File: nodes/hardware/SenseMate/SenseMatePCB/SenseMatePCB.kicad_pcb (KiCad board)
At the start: 2 copper layers, 40.6 x 67.8 mm, 14 parts, among them J1 Conn_01x04, M1 Motor_DC, Q1 2SC1815, Q2 2SC1815, SW5 SW_DPDT_x2

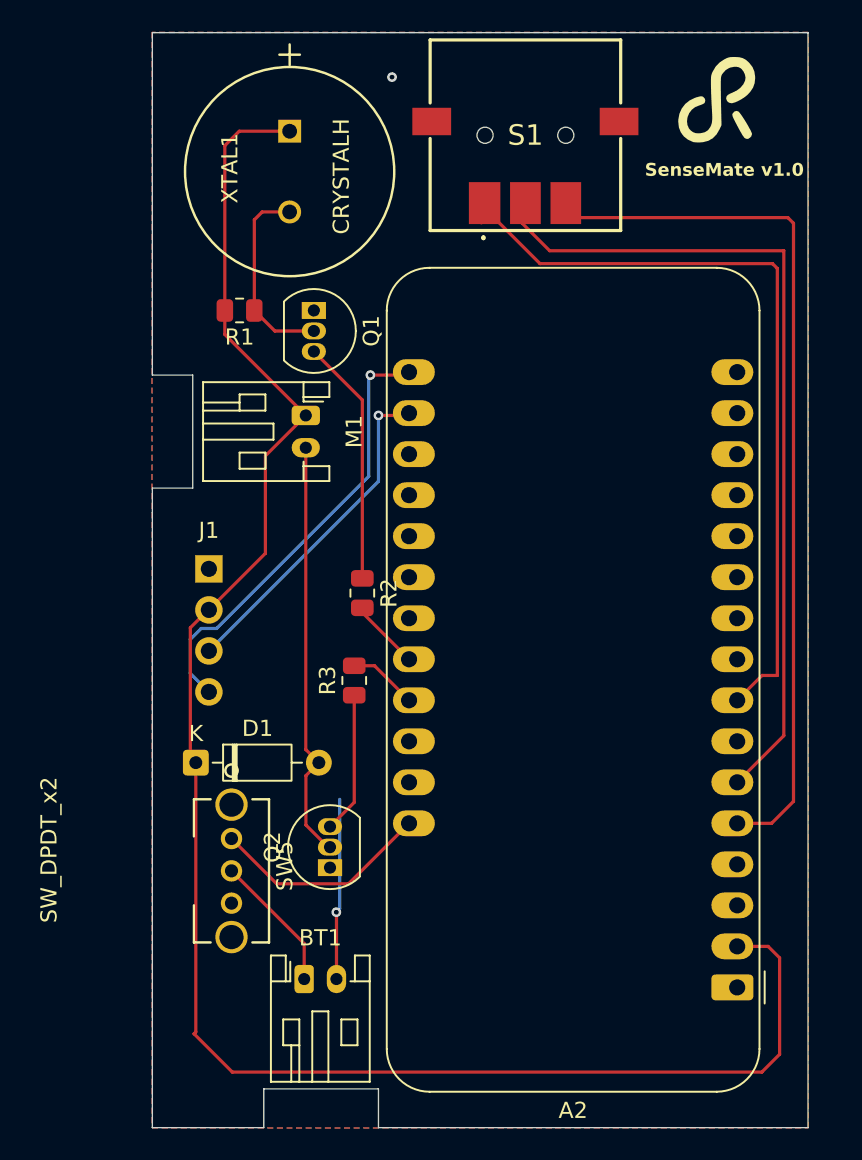
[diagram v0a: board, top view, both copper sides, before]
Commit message: some silkscreen writing movement
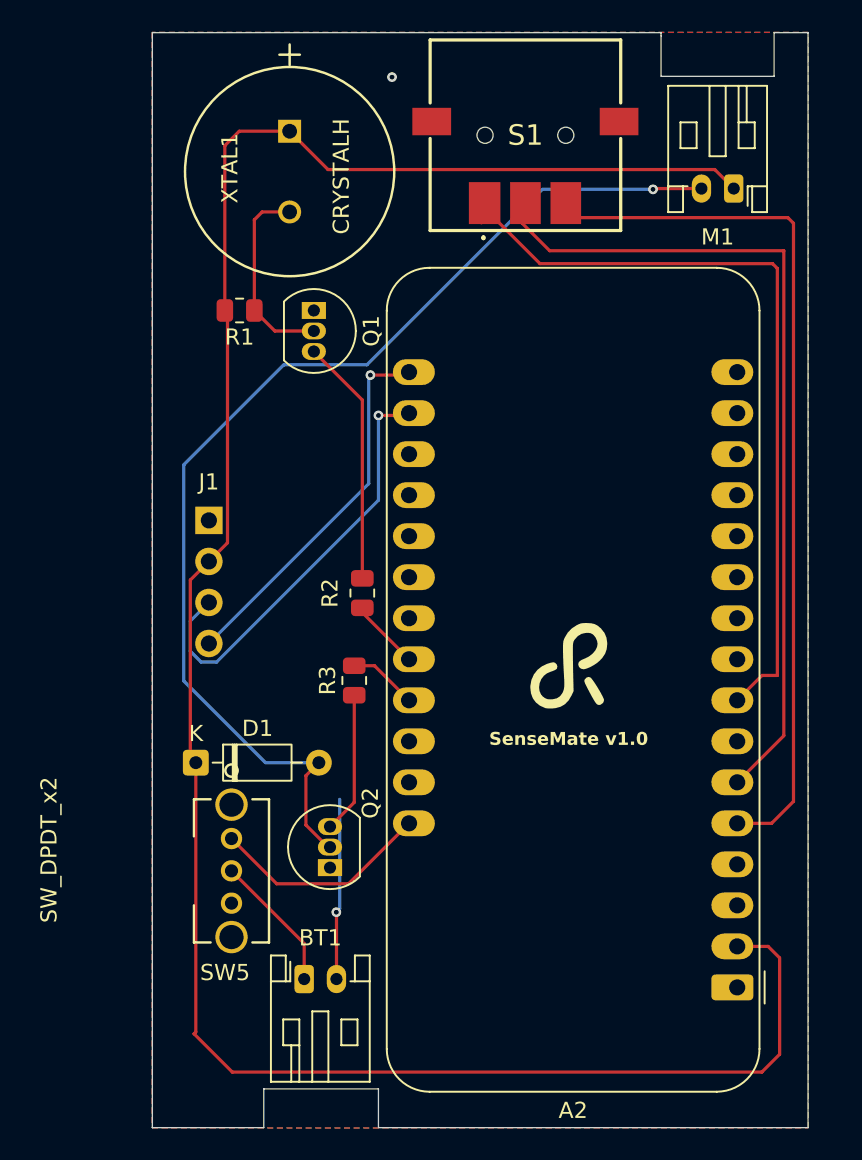
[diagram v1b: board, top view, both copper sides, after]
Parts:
- moved G*** 36.2 mm to (107.8, 85.5)
- moved M1 30.0 mm to (115.5, 56.0), turned to 180 degrees
- moved J1 3.00 mm to (83.0, 76.5)
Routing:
- net Net-(D1-A): track 26.1 -> 69.2 mm, vias 0 -> 1
- net +3V3: track 111.2 -> 136.1 mm
- net Net-(A2-SCL): track 21.0 -> 26.8 mm
- net Net-(A2-SDA): track 27.7 -> 23.3 mm
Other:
- outline, holes or cut-outs redrawn

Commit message: added gerberfiles issue#7
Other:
- board text added: "10/06/25 SenseMate v1.0"
- board text added: "JLCJCLJCLJLC"
- board text removed: "SenseMate v1.0"
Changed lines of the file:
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@@
 			(plot_on_all_layers_selection 0x00000000_00000000_00000000_00000000)
 			(disableapertmacros no)
-			(usegerberextensions no)
-			(usegerberattributes yes)
-			(usegerberadvancedattributes yes)
-			(creategerberjobfile yes)
+			(usegerberextensions yes)
+			(usegerberattributes no)
+			(usegerberadvancedattributes no)
+			(creategerberjobfile no)
 			(dashed_line_dash_ratio 12.000000)
 			(dashed_line_gap_ratio 3.000000)
@@
 			(outputformat 1)
 			(mirror no)
-			(drillshape 1)
+			(drillshape 0)
 			(scaleselection 1)
-			(outputdirectory "")
+			(outputdirectory "gerbers/")
 		)
 	)
@@
 		(layer "User.4")
 	)
-	(gr_text "SenseMate v1.0"
-		(at 100.347416 90.495713 0)
+	(gr_text "JLCJCLJCLJLC"
+		(at 100 101.5 0)
+		(layer "F.SilkS")
+		(effects
+			(font
+				(size 1 1)
+				(thickness 0.1)
+			)
+			(justify left bottom)
+		)
+	)
+	(gr_text "10/06/25 SenseMate v1.0"
+		(at 97.5 90 0)
 		(layer "F.SilkS")
 		(effects

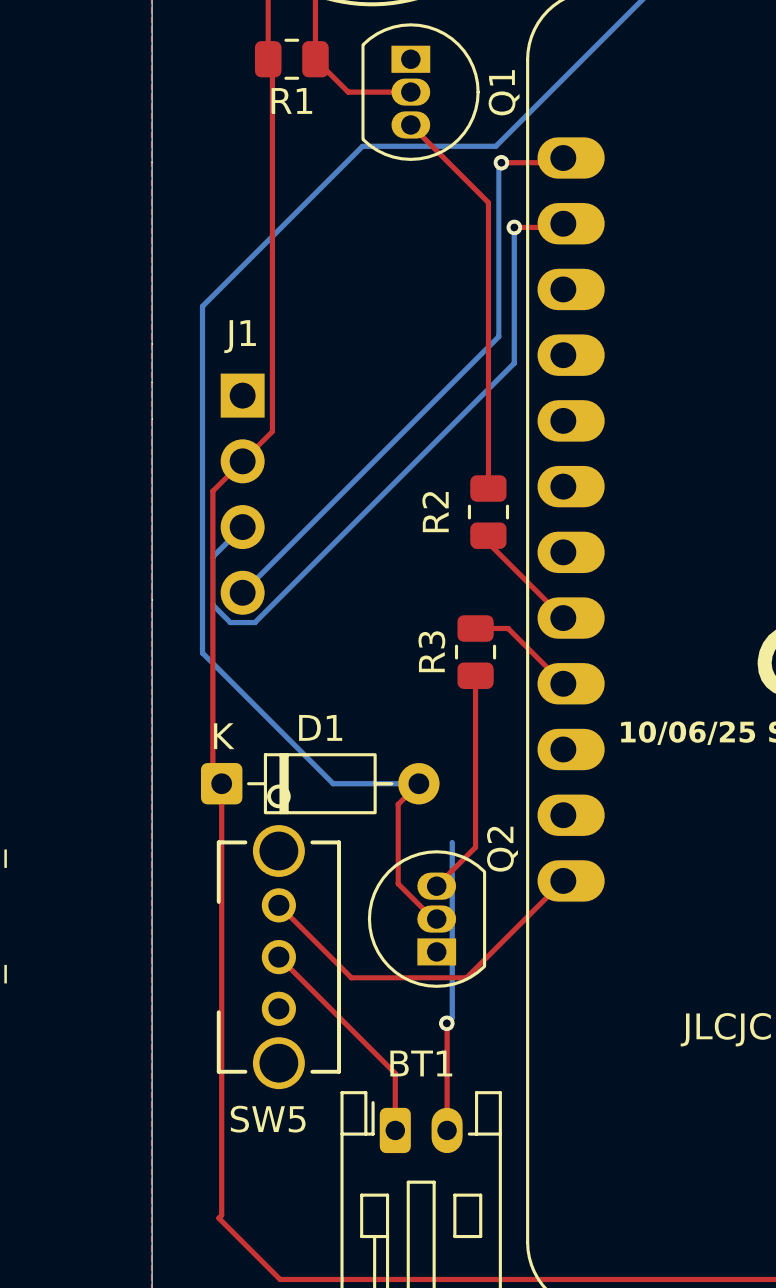
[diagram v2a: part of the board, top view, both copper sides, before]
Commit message: Fix DRC issues and create release gerber
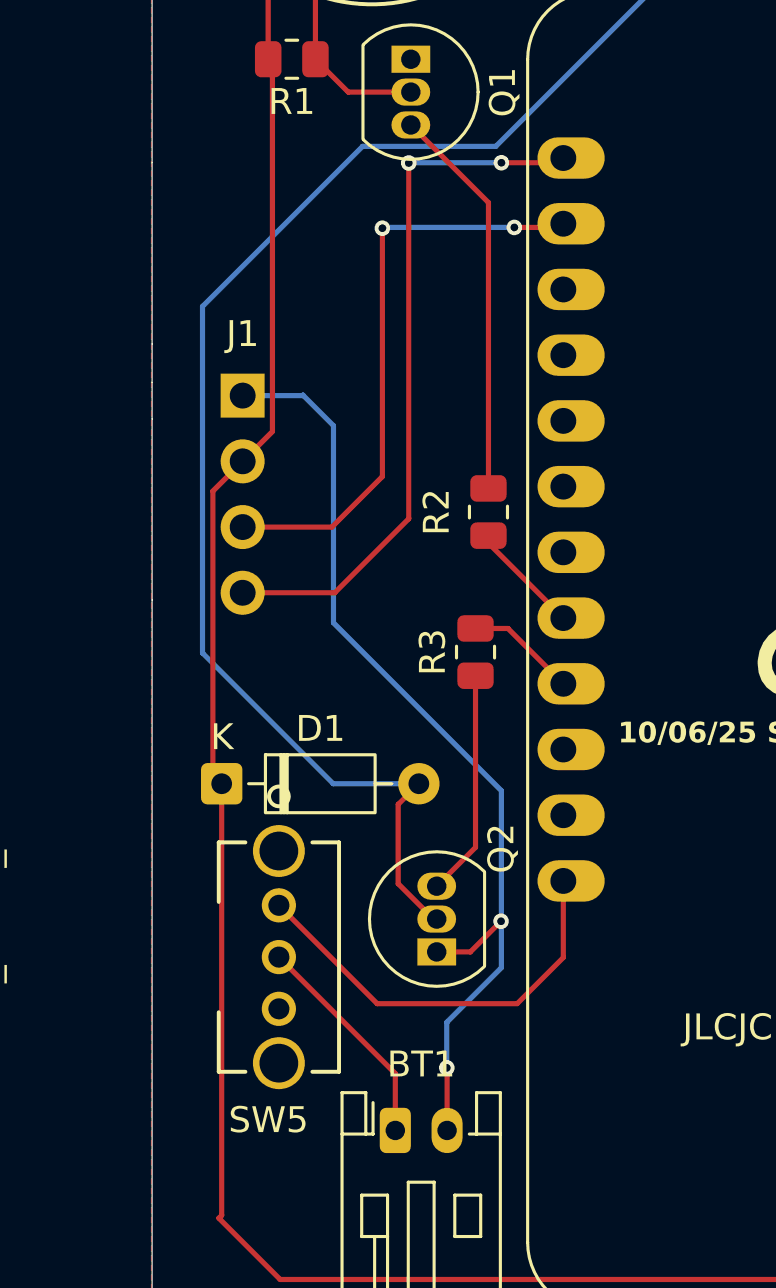
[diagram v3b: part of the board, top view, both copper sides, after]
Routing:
- net GND: track 11.2 -> 37.9 mm, vias 2 -> 3
- net Net-(A2-SDA): track 23.3 -> 27.7 mm, vias 1 -> 2
- net Net-(A2-SCL): track 26.8 -> 22.9 mm, vias 1 -> 2
- net Net-(A2-VBAT): track 13.7 -> 16.3 mm
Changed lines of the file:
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@@
 			(drillshape 0)
 			(scaleselection 1)
-			(outputdirectory "gerbers/")
+			(outputdirectory "gerber_v1_0/")
 		)
 	)
@@
 	)
 	(segment
-		(start 87.200001 99)
-		(end 91.650901 99)
+		(start 84.4 96.199999)
+		(end 88.2 99.999999)
 		(width 0.2)
 		(layer "F.Cu")
@@
 	)
 	(segment
-		(start 91.650901 99)
-		(end 95.3939 95.257001)
+		(start 93.610001 99.999999)
+		(end 95.3939 98.2161)
 		(width 0.2)
 		(layer "F.Cu")
@@
 	)
 	(segment
-		(start 84.4 96.199999)
-		(end 87.200001 99)
+		(start 88.2 99.999999)
+		(end 93.610001 99.999999)
+		(width 0.2)
+		(layer "F.Cu")
+		(net 16)
+	)
+	(segment
+		(start 95.3939 98.2161)
+		(end 95.3939 95.257001)
 		(width 0.2)
 		(layer "F.Cu")
@@
 	)
 	(segment
-		(start 90.9 100.77)
-		(end 90.89 100.76)
+		(start 91.802372 98)
+		(end 90.5 98)
 		(width 0.2)
 		(layer "F.Cu")
@@
 	(segment
 		(start 90.9 104.9)
-		(end 90.9 100.77)
+		(end 90.9 102.49)
+		(width 0.2)
+		(layer "F.Cu")
+		(net 25)
+	)
+	(segment
+		(start 92.986186 96.816186)
+		(end 91.802372 98)
+		(width 0.2)
+		(layer "F.Cu")
+		(net 25)
+	)
+	(segment
+		(start 90.9 102.49)
+		(end 90.89 102.48)
 		(width 0.2)
 		(layer "F.Cu")
@@
 	)
 	(via
-		(at 94.34 49.05)
+		(at 92.986186 96.816186)
 		(size 0.6)
 		(drill 0.3)
 		(layers "F.Cu" "B.Cu")
-		(free yes)
 		(net 25)
 	)
 	(via
-		(at 90.89 100.76)
+		(at 90.89 102.48)
 		(size 0.6)
 		(drill 0.3)
@@
 		(net 25)
 	)
+	(via
+		(at 94.34 49.05)
+		(size 0.6)
+		(drill 0.3)
+		(layers "F.Cu" "B.Cu")
+		(free yes)
+		(net 25)
+	)
+	(segment
+		(start 85.31 76.5)
+		(end 83 76.5)
+		(width 0.2)
+		(layer "B.Cu")
+		(net 25)
+	)
+	(segment
+		(start 85.33 76.48)
+		(end 85.31 76.5)
+		(width 0.2)
+		(layer "B.Cu")
+		(net 25)
+	)
+	(segment
+		(start 93 91.77)
+		(end 86.51 85.28)
+		(width 0.2)
+		(layer "B.Cu")
+		(net 25)
+	)
+	(segment
+		(start 93 96.91)
+		(end 93 91.77)
+		(width 0.2)
+		(layer "B.Cu")
+		(net 25)
+	)
+	(segment
+		(start 93 98.61)
+		(end 93 96.91)
+		(width 0.2)
+		(layer "B.Cu")
+		(net 25)
+	)
+	(segment
+		(start 93 96.91)
+		(end 93 96.83)
+		(width 0.2)
+		(layer "B.Cu")
+		(net 25)
+	)
+	(segment
+		(start 86.51 85.28)
+		(end 86.51 77.66)
+		(width 0.2)
+		(layer "B.Cu")
+		(net 25)
+	)
+	(segment
+		(start 90.89 102.48)
+		(end 90.89 100.72)
+		(width 0.2)
+		(layer "B.Cu")
+		(net 25)
+	)
 	(segment
-		(start 90.89 100.76)
-		(end 91.1 100.55)
+		(start 93 96.83)
+		(end 92.986186 96.816186)
 		(width 0.2)
 		(layer "B.Cu")
@@
 	)
 	(segment
-		(start 91.1 100.55)
-		(end 91.1 93.77)
+		(start 86.51 77.66)
+		(end 85.33 76.48)
+		(width 0.2)
+		(layer "B.Cu")
+		(net 25)
+	)
+	(segment
+		(start 90.89 100.72)
+		(end 93 98.61)
 		(width 0.2)
 		(layer "B.Cu")
@@
 	)
 	(segment
+		(start 88.4 70.03)
+		(end 88.4 79.63)
+		(width 0.2)
+		(layer "F.Cu")
+		(net 34)
+	)
+	(segment
 		(start 95.250901 70)
 		(end 95.3939 69.857001)
@@
 	)
 	(segment
+		(start 88.4 79.63)
+		(end 86.45 81.58)
+		(width 0.2)
+		(layer "F.Cu")
+		(net 34)
+	)
+	(segment
 		(start 93.5 70)
 		(end 95.250901 70)
@@
 		(net 34)
 	)
+	(segment
+		(start 86.45 81.58)
+		(end 83 81.58)
+		(width 0.2)
+		(layer "F.Cu")
+		(net 34)
+	)
 	(via
 		(at 93.5 70)
@@
 		(net 34)
 	)
-	(segment
-		(start 93.5 75.24776)
-		(end 93.5 70)
-		(width 0.2)
-		(layer "B.Cu")
+	(via
+		(at 88.4 70.03)
+		(size 0.6)
+		(drill 0.3)
+		(layers "F.Cu" "B.Cu")
 		(net 34)
 	)
 	(segment
-		(start 81.849 84.59676)
-		(end 82.52324 85.271)
+		(start 93.5 70)
+		(end 88.43 70)
 		(width 0.2)
 		(layer "B.Cu")
@@
 	)
 	(segment
-		(start 83 81.58)
-		(end 81.849 82.731)
+		(start 88.43 70)
+		(end 88.4 70.03)
 		(width 0.2)
 		(layer "B.Cu")
@@
 	)
 	(segment
-		(start 83.47676 85.271)
-		(end 93.5 75.24776)
+		(start 89.42 81.26)
+		(end 89.42 67.51)
 		(width 0.2)
-		(layer "B.Cu")
-		(net 34)
+		(layer "F.Cu")
+		(net 35)
 	)
 	(segment
-		(start 81.849 82.731)
-		(end 81.849 84.59676)
+		(start 95.210901 67.5)
+		(end 95.3939 67.317001)
 		(width 0.2)
-		(layer "B.Cu")
-		(net 34)
+		(layer "F.Cu")
+		(net 35)
 	)
 	(segment
-		(start 82.52324 85.271)
-		(end 83.47676 85.271)
+		(start 93 67.5)
+		(end 95.210901 67.5)
 		(width 0.2)
-		(layer "B.Cu")
-		(net 34)
+		(layer "F.Cu")
+		(net 35)
 	)
 	(segment
-		(start 95.210901 67.5)
-		(end 95.3939 67.317001)
+		(start 86.56 84.12)
+		(end 89.42 81.26)
 		(width 0.2)
 		(layer "F.Cu")
@@
 	)
 	(segment
-		(start 93 67.5)
-		(end 95.210901 67.5)
+		(start 83 84.12)
+		(end 86.56 84.12)
 		(width 0.2)
 		(layer "F.Cu")
@@
 	)
 	(via
+		(at 89.42 67.51)
+		(size 0.6)
+		(drill 0.3)
+		(layers "F.Cu" "B.Cu")
+		(net 35)
+	)
+	(via
 		(at 93 67.5)
 		(size 0.6)
@@
 	)
 	(segment
-		(start 92.899 67.601)
-		(end 93 67.5)
+		(start 93 67.5)
+		(end 89.43 67.5)
 		(width 0.2)
 		(layer "B.Cu")
@@
 	)
 	(segment
-		(start 92.899 74.221)
-		(end 92.899 67.601)
+		(start 92.899 67.601)
+		(end 93 67.5)
 		(width 0.2)
 		(layer "B.Cu")
@@
 	)
 	(segment
-		(start 83 84.12)
-		(end 92.899 74.221)
+		(start 83.42 84.58)
+		(end 83.5 84.5)
 		(width 0.2)
 		(layer "B.Cu")
@@
 	)
 	(segment
-		(start 83.42 84.58)
-		(end 83.5 84.5)
+		(start 89.43 67.5)
+		(end 89.42 67.51)
 		(width 0.2)
 		(layer "B.Cu")
